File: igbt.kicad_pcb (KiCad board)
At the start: 2 copper layers, 160 x 99.7 mm, 52 parts, among them J1 A_Top, J10 Motor, J2 A_Bottom, J3 B_Top, J4 B_Bottom, J5 C_Top, J6 C_Bottom, J7 Sense_AC_B, J8 Sense_AC_A, J9 DC_Sense, Q1 IRG4PF50W, Q2 IRG4PF50W, Q3 IRG4PF50W, Q4 IRG4PF50W, Q5 IRG4PF50W, Q6 IRG4PF50W, U1 ACS758xCB-050B-PFF, U2 ACS758xCB-050B-PFF

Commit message: Fully insulated gate drive
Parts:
- removed J5: C_Top, Connector_PinHeader_2.54mm:PinHeader_1x02_P2.54mm_Vertical
- removed J6: C_Bottom, Connector_PinHeader_2.54mm:PinHeader_1x02_P2.54mm_Vertical
- added C1: 4u7, Capacitor_SMD:C_0805_2012Metric, B.Cu at (80.9, 19.9)
- added C2: 4u7, Capacitor_SMD:C_0805_2012Metric, B.Cu at (77.9, 35.2)
- added C3: 4u7, Capacitor_SMD:C_0805_2012Metric, B.Cu at (74.1, 21.9)
- added C6: 4u7, Capacitor_SMD:C_0805_2012Metric, B.Cu at (77.5, 153.0)
- added C7: 4u7, Capacitor_SMD:C_0805_2012Metric, B.Cu at (77.5, 170.2)
- added C8: 4u7, Capacitor_SMD:C_0805_2012Metric, B.Cu at (77.5, 186.1)
- added R10: R, Capacitor_SMD:C_0805_2012Metric, B.Cu at (187.3, 113.0)
- added R11: R, Capacitor_SMD:C_0805_2012Metric, B.Cu at (194.9, 87.0)
- added R12: 1k, Resistor_SMD:R_0805_2012Metric, B.Cu at (74.1, 18.0)
- added R13: R, Capacitor_SMD:C_0805_2012Metric, B.Cu at (105.1, 113.0)
- added R14: R, Capacitor_SMD:C_0805_2012Metric, B.Cu at (103.6, 1.28)
- added R15: 330, Resistor_SMD:R_0805_2012Metric, B.Cu at (81.3, 35.2)
- added R16: R, Capacitor_SMD:C_0805_2012Metric, B.Cu at (146.7, 112.4)
- added R17: R, Capacitor_SMD:C_0805_2012Metric, B.Cu at (80.9, 18.0)
- added R18: 1k, Resistor_SMD:R_0805_2012Metric, F.Cu at (193.1, 193.0)
- added R19: 1k, Resistor_SMD:R_0805_2012Metric, F.Cu at (277.9, 55.8)
- added R20: 330, Resistor_SMD:R_0805_2012Metric, F.Cu at (266.7, 58.3)
- added R21: 1k, Resistor_SMD:R_0805_2012Metric, F.Cu at (268.6, 56.0)
- added R22: 1k, Resistor_SMD:R_0805_2012Metric, F.Cu at (263.3, 58.3)
- added R23: 330, Resistor_SMD:R_0805_2012Metric, B.Cu at (48.3, 153.4)
- added R24: 1k, Resistor_SMD:R_0805_2012Metric, B.Cu at (62.9, 155.6)
- added R25: 1k, Resistor_SMD:R_0805_2012Metric, B.Cu at (77.5, 157.5)
- added R26: 330, Resistor_SMD:R_0805_2012Metric, B.Cu at (48.3, 171.8)
- added R27: 1k, Resistor_SMD:R_0805_2012Metric, B.Cu at (62.9, 174.0)
- added R28: 1k, Resistor_SMD:R_0805_2012Metric, B.Cu at (77.5, 175.3)
- added R29: 330, Resistor_SMD:R_0805_2012Metric, B.Cu at (48.3, 188.3)
- added R30: 1k, Resistor_SMD:R_0805_2012Metric, B.Cu at (62.9, 190.5)
- added R31: 1k, Resistor_SMD:R_0805_2012Metric, B.Cu at (77.5, 191.8)
- added R9: 1k, Resistor_SMD:R_0805_2012Metric, B.Cu at (80.9, 21.9)
- added U10: TC4420, Package_DIP:DIP-8_W7.62mm_LongPads, B.Cu at (66.0, 157.5)
- added U11: 6N137, Package_DIP:DIP-8_W7.62mm_LongPads, B.Cu at (52.1, 175.3)
- added U12: TC4420, Package_DIP:DIP-8_W7.62mm_LongPads, B.Cu at (66.0, 175.3)
- added U13: 6N137, Package_DIP:DIP-8_W7.62mm_LongPads, B.Cu at (52.1, 191.8)
- added U14: TC4420, Package_DIP:DIP-8_W7.62mm_LongPads, B.Cu at (66.0, 191.8)
- added U3: 6N137, Package_DIP:DIP-8_W7.62mm_LongPads, B.Cu at (214.0, 102.9)
- added U4: TC4420, Package_DIP:DIP-8_W7.62mm_LongPads, B.Cu at (201.3, 102.9)
- added U5: 6N137, Package_DIP:DIP-8_W7.62mm_LongPads, B.Cu at (207.6, 81.3)
- added U6: TC4420, Package_DIP:DIP-8_W7.62mm_LongPads, B.Cu at (214.0, 88.3)
- added U7: 6N137, Package_DIP:DIP-8_W7.62mm_LongPads, B.Cu at (116.2, 101.6)
- added U8: TC4420, Package_DIP:DIP-8_W7.62mm_LongPads, F.Cu at (118.7, 89.5)
- added U9: 6N137, Package_DIP:DIP-8_W7.62mm_LongPads, B.Cu at (52.1, 157.5)
- D1, D2, D3: value BYV79-100 -> 5V1; footprint Package_TO_SOT_THT:TO-220-2_Horizontal_TabUp -> Diode_SMD:D_MiniMELF
- D4, D5, D6: value BYV79-100 -> 5V1; footprint Package_TO_SOT_THT:TO-220-2_Horizontal_TabUp -> Diode_SMD:D_MiniMELF; moved to B.Cu
- J1: value A_Top -> PWM; footprint Connector_PinHeader_2.54mm:PinHeader_1x02_P2.54mm_Vertical -> Connector_PinHeader_2.54mm:PinHeader_1x08_P2.54mm_Vertical; moved to F.Cu
- J2: value A_Bottom -> PwrGate_A
- J3: value B_Top -> PwrGate_B; moved to F.Cu
- J4: value B_Bottom -> PwrGate_C
- R7: value 100k -> 330; footprint Resistor_SMD:R_1206_3216Metric -> Resistor_SMD:R_0805_2012Metric
- R8: value 1k -> 100k; footprint Resistor_SMD:R_0805_2012Metric -> Resistor_SMD:R_2816_7142Metric
- moved D3 176.0 mm to (264.3, 56.2), turned to 0 degrees
- moved J3 136.1 mm to (240.4, 32.3)
- moved J9 128.0 mm to (340.4, 115.6)
- moved H3 128.0 mm to (346.1, 41.3)
- moved J8 128.0 mm to (332.1, 60.3)
- moved R7 128.0 mm to (337.2, 43.8)
- moved TP1 128.0 mm to (339.7, 95.2)
- moved TP6 128.0 mm to (325.8, 41.9)
- moved TP8 128.0 mm to (328.3, 48.9)
- moved C4 128.0 mm to (337.2, 70.5)
- moved H4 128.0 mm to (346.1, 130.8)
- moved R8 128.0 mm to (341.9, 111.1)
- moved TP3 128.0 mm to (330.2, 116.8)
- moved TP7 128.0 mm to (330.8, 128.3)
- moved U1 128.0 mm to (337.2, 65.7)
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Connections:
- D1 pad 1: /DC_Link -> Net-(D1-Pad1)
- D1 pad 2: Net-(D1-Pad2) -> /TopDriver/Source
- D2 pad 1: Net-(D1-Pad2) -> Net-(D2-Pad1)
- D2 pad 2: /DC_Link_GND -> /sheet5F55AA82/Source
- D3 pad 1: /DC_Link -> Net-(D3-Pad1)
- D3 pad 2: Net-(D3-Pad2) -> /sheet5F5616DC/Source
- D4 pad 1: Net-(D3-Pad2) -> Net-(D4-Pad1)
- D5 pad 1: /DC_Link -> Net-(D5-Pad1)
- D5 pad 2: Net-(D5-Pad2) -> /DC_Link_GND
- D6 pad 1: Net-(D5-Pad2) -> Net-(D6-Pad1)
- J1 pad 1: Net-(D1-Pad2) -> /DC_Link_GND
- J1 pad 2: Net-(J1-Pad2) -> /sheet5F641D5F/Cathode
- J2 pad 1: /DC_Link_GND -> /TopDriver/Source
- J2 pad 2: Net-(J2-Pad2) -> /TopDriver/Power
- J3 pad 1: Net-(D3-Pad2) -> /sheet5F55AA82/Source
- J3 pad 2: Net-(J3-Pad2) -> /sheet5F55AA82/Power
- J4 pad 1: /DC_Link_GND -> /sheet5F5616DC/Source
- J4 pad 2: Net-(J4-Pad2) -> /sheet5F5616DC/Power
- J9 pad 2: /bus_sense -> (no net)
- Q1 pad 1: Net-(J1-Pad2) -> Net-(Q1-Pad1)
- Q1 pad 2: /DC_Link -> Net-(Q1-Pad2)
- Q1 pad 3: Net-(D1-Pad2) -> /TopDriver/Source
- Q2 pad 1: Net-(J2-Pad2) -> Net-(Q2-Pad1)
- Q2 pad 2: Net-(D1-Pad2) -> /TopDriver/Source
- Q3 pad 1: Net-(J3-Pad2) -> Net-(Q3-Pad1)
- Q3 pad 2: /DC_Link -> Net-(Q1-Pad2)
- Q3 pad 3: Net-(D3-Pad2) -> /sheet5F55AA82/Source
- Q4 pad 1: Net-(J4-Pad2) -> Net-(Q4-Pad1)
- Q4 pad 2: Net-(D3-Pad2) -> /sheet5F55AA82/Source
- Q5 pad 2: /DC_Link -> Net-(Q1-Pad2)
- Q5 pad 3: Net-(D5-Pad2) -> /sheet5F5616DC/Source
- Q6 pad 2: Net-(D5-Pad2) -> /sheet5F5616DC/Source
- R1 pad 1: Net-(J1-Pad2) -> Net-(Q1-Pad1)
- R1 pad 2: Net-(D1-Pad2) -> /TopDriver/Source
- R2 pad 1: Net-(J2-Pad2) -> Net-(Q2-Pad1)
- R3 pad 1: Net-(J3-Pad2) -> Net-(Q3-Pad1)
- R3 pad 2: Net-(D3-Pad2) -> /sheet5F55AA82/Source
- R4 pad 1: Net-(J4-Pad2) -> Net-(Q4-Pad1)
- R5 pad 2: Net-(D5-Pad2) -> /sheet5F5616DC/Source
- R7 pad 1: /bus_sense -> Net-(R7-Pad1)
- R7 pad 2: /DC_Link -> +5V
- R8 pad 1: /DC_Link_GND -> (no net)
- R8 pad 2: /bus_sense -> (no net)
- TP2 pad 1: /DC_Link -> Net-(Q1-Pad2)
- TP5 pad 1: Net-(D5-Pad2) -> /sheet5F5616DC/Source
- TP6 pad 1: /DC_Link -> Net-(Q1-Pad2)
- TP8 pad 1: /DC_Link -> Net-(Q1-Pad2)
- TP9 pad 1: /DC_Link -> Net-(Q1-Pad2)
- U1 pad 4: Net-(D1-Pad2) -> /TopDriver/Source
- U2 pad 4: Net-(D3-Pad2) -> /sheet5F55AA82/Source
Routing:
- net /DC_Link_GND: track 279.0 -> 37.5 mm
- net /DC_Link: track 168.2 -> 0.00 mm
- net Net-(D1-Pad2): track 164.9 -> 0.00 mm
- net Net-(D3-Pad2): track 113.9 -> 0.00 mm
- net Net-(D5-Pad2): track 107.3 -> 0.00 mm
- net /bus_sense: track 80.5 -> 0.00 mm
- net Net-(R7-Pad1): track 0.00 -> 76.1 mm
- net Net-(D4-Pad1): track 0.00 -> 32.0 mm
- net Net-(D6-Pad1): track 0.00 -> 31.1 mm
- net /sheet5F641D5F/Gate: track 0.00 -> 19.6 mm
- net /sheet5F64C50D/Power: track 0.00 -> 15.7 mm
- net /sheet5F641D5F/Power: track 0.00 -> 14.4 mm
- net Net-(Q1-Pad2): track 0.00 -> 11.5 mm
- net Net-(D5-Pad1): track 0.00 -> 10.5 mm
- net Net-(J2-Pad2): track 10.1 -> 0.00 mm
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- removed copper zone on B.Cu, net /DC_Link
- removed copper zone on B.Cu, net /DC_Link_GND
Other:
- board outline removed

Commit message: Driver placed
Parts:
- D1, D2, D3, J3, R18, R19, R20, R21, R22, U8: moved to B.Cu
- moved R19 165.7 mm to (114.9, 85.4), turned to 270 degrees
- moved D2 161.1 mm to (121.3, 87.0)
- moved H3 156.7 mm to (238.8, 155.4)
- moved R7 156.4 mm to (181.1, 54.1), turned to 0 degrees
- moved R18 145.2 mm to (116.2, 69.8)
- moved J3 140.9 mm to (112.3, 90.9)
- moved J8 138.9 mm to (193.4, 67.4)
- moved TP1 138.9 mm to (201.0, 102.4)
- moved C4 138.9 mm to (198.5, 77.6)
- moved U1 138.9 mm to (198.5, 72.8)
- moved U9 133.3 mm to (182.1, 128.0), turned to 90 degrees
- moved R23 131.5 mm to (178.0, 131.8), turned to 180 degrees
- moved U10 123.9 mm to (182.1, 114.0), turned to 90 degrees
- moved R24 123.5 mm to (180.2, 117.2), turned to 180 degrees
- moved R12 123.0 mm to (177.9, 83.9), turned to 270 degrees
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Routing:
- net /TopDriver/Source: track 0.00 -> 131.1 mm
- net /sheet5F55AA82/Source: track 0.00 -> 87.7 mm
- net /sheet5F5616DC/Source: track 0.00 -> 86.9 mm
- net Net-(R7-Pad1): track 76.1 -> 0.00 mm
- net /DC_Link_GND: track 37.5 -> 74.4 mm
- net Net-(Q4-Pad1): track 0.00 -> 17.7 mm
- net /sheet5F5616DC/Power: track 0.00 -> 17.4 mm
- net Net-(Q2-Pad1): track 0.00 -> 17.4 mm
- net Net-(Q6-Pad1): track 0.00 -> 17.0 mm
- net /TopDriver/Power: track 0.00 -> 15.8 mm
- net Net-(Q1-Pad1): track 0.00 -> 15.8 mm
- net Net-(D4-Pad1): track 32.0 -> 16.4 mm
- net /sheet5F5616DC/Gate: track 0.00 -> 15.5 mm
- net /sheet5F55AA82/Power: track 0.00 -> 15.1 mm
- net Net-(Q5-Pad1): track 0.00 -> 14.3 mm
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
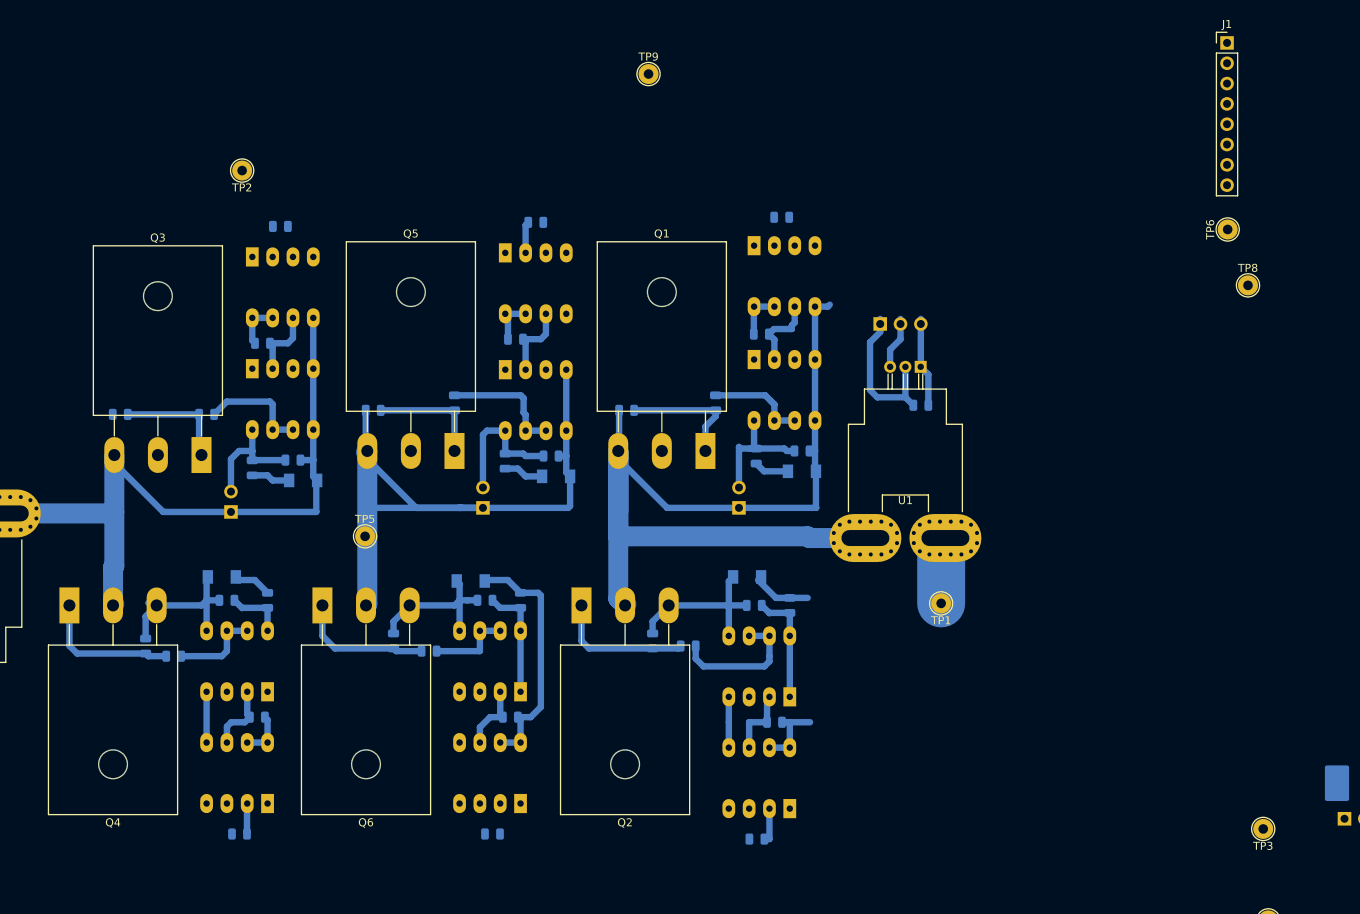
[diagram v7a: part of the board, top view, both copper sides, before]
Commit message: Separate drive connectors per phase
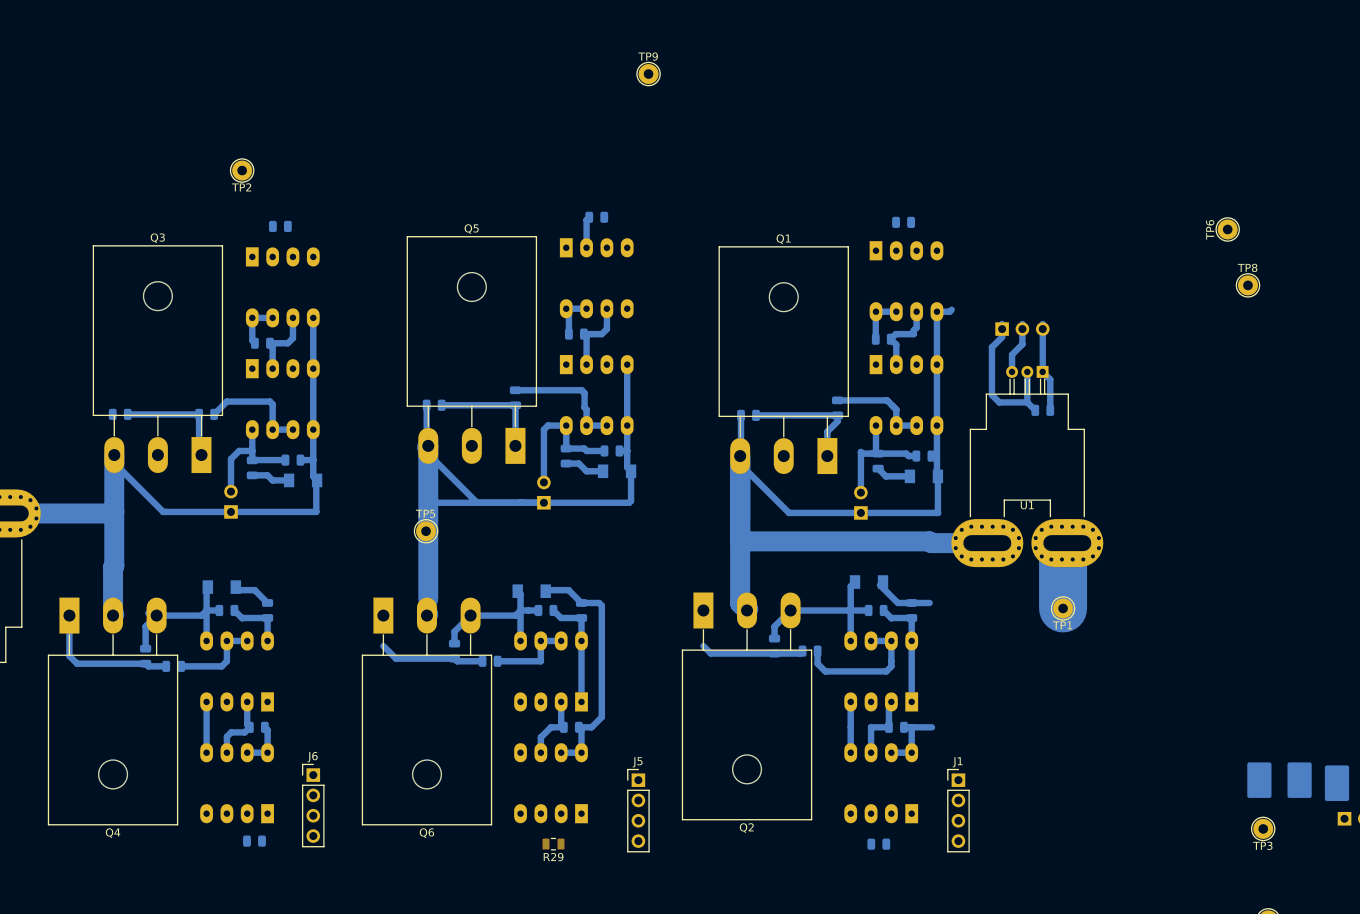
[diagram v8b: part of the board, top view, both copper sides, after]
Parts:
- added J5: PWM, Connector_PinHeader_2.54mm:PinHeader_1x04_P2.54mm_Vertical, F.Cu at (163.2, 124.5)
- added J6: PWM, Connector_PinHeader_2.54mm:PinHeader_1x04_P2.54mm_Vertical, F.Cu at (122.6, 123.8)
- added R32: 1k, Resistor_SMD:R_2816_7142Metric, B.Cu at (243.3, 124.5)
- J1: footprint Connector_PinHeader_2.54mm:PinHeader_1x08_P2.54mm_Vertical -> Connector_PinHeader_2.54mm:PinHeader_1x04_P2.54mm_Vertical
- R29: moved to F.Cu
- moved J1 98.1 mm to (203.2, 124.5)
- moved C1 15.3 mm to (198.9, 83.9)
- moved C4 15.3 mm to (213.7, 78.2)
- moved C6 15.3 mm to (192.9, 103.3)
- moved D1 15.3 mm to (198.9, 86.5)
- moved D4 15.3 mm to (192.0, 99.7)
- moved J2 15.3 mm to (191.0, 91.1)
- moved J8 15.3 mm to (208.7, 68.1)
- moved Q1 15.3 mm to (186.8, 83.9)
- moved Q2 15.3 mm to (171.3, 103.3)
- moved R12 15.3 mm to (193.2, 84.6)
- moved R24 15.3 mm to (195.5, 117.9)
- moved R25 15.3 mm to (197.4, 103.3)
- moved R7 15.3 mm to (196.3, 54.7)
- moved TP1 15.3 mm to (216.3, 103.0)
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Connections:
- J1 pad 4: /sheet5F647249/Cathode -> /TopDriver/PowerLed
- J9 pad 2: (no net) -> /bus_sense
- R15 pad 2: +5V -> /sheet5F55AA82/PowerLed
- R20 pad 2: +5V -> /sheet5F5616DC/PowerLed
- R23 pad 2: +5V -> /TopDriver/PowerLed
- R26 pad 2: +5V -> /sheet5F55AA82/PowerLed
- R29 pad 2: +5V -> /sheet5F5616DC/PowerLed
- R7 pad 2: +5V -> /TopDriver/PowerLed
- R8 pad 1: (no net) -> /bus_sense
- R8 pad 2: (no net) -> Net-(Q1-Pad2)
- U10 pad 3: (no net) -> Net-(U10-Pad3)
- U11 pad 1: (no net) -> Net-(U11-Pad1)
- U11 pad 4: (no net) -> Net-(U11-Pad4)
- U12 pad 3: (no net) -> Net-(U12-Pad3)
- U13 pad 1: (no net) -> Net-(U13-Pad1)
- U13 pad 4: (no net) -> Net-(U13-Pad4)
- U14 pad 3: (no net) -> Net-(U14-Pad3)
- U3 pad 1: (no net) -> Net-(U3-Pad1)
- U3 pad 4: (no net) -> Net-(U3-Pad4)
- U4 pad 3: (no net) -> Net-(U4-Pad3)
- U5 pad 1: (no net) -> Net-(U5-Pad1)
- U5 pad 4: (no net) -> Net-(U5-Pad4)
- U6 pad 3: (no net) -> Net-(U6-Pad3)
- U7 pad 1: (no net) -> Net-(U7-Pad1)
- U7 pad 4: (no net) -> Net-(U7-Pad4)
- U8 pad 3: (no net) -> Net-(U8-Pad3)
- U9 pad 1: (no net) -> Net-(U9-Pad1)
- U9 pad 4: (no net) -> Net-(U9-Pad4)
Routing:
- net Net-(Q2-Pad1): track 17.4 -> 12.9 mm
- net Net-(R23-Pad1): track 4.44 -> 0.00 mm
- net Net-(Q6-Pad1): track 17.0 -> 13.2 mm
- net Net-(R26-Pad1): track 3.82 -> 0.04 mm
